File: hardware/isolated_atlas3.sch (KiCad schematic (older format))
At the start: 14 parts, among them J501 CONN_01X02, U501 adm3260, U502 ATLAS_SENSOR

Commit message: Fix SSOP-20 width on the isolator.
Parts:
- U501: footprint SMD_Packages:SSOP-20 -> conservify:SSOP20-53
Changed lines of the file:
@@
 F 0 "U501" H 4400 2750 60  0000 C CNN
 F 1 "adm3260" H 4400 2900 60  0000 C CNN
-F 2 "SMD_Packages:SSOP-20" H 4400 2900 60  0001 C CNN
+F 2 "conservify:SSOP20-53" H 4400 2900 60  0001 C CNN
 F 3 "" H 4400 2900 60  0001 C CNN
 F 4 "584-ADM3260ARSZ" H 0   0   50  0001 C CNN "spn1"

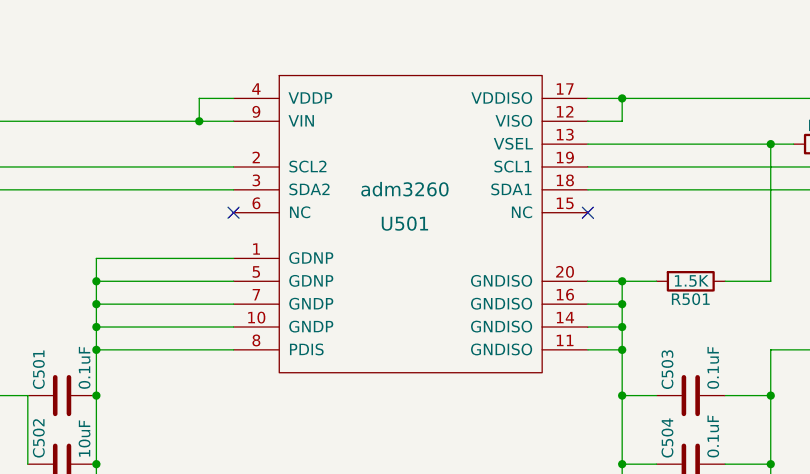
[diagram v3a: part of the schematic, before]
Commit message: Fixing some component names.
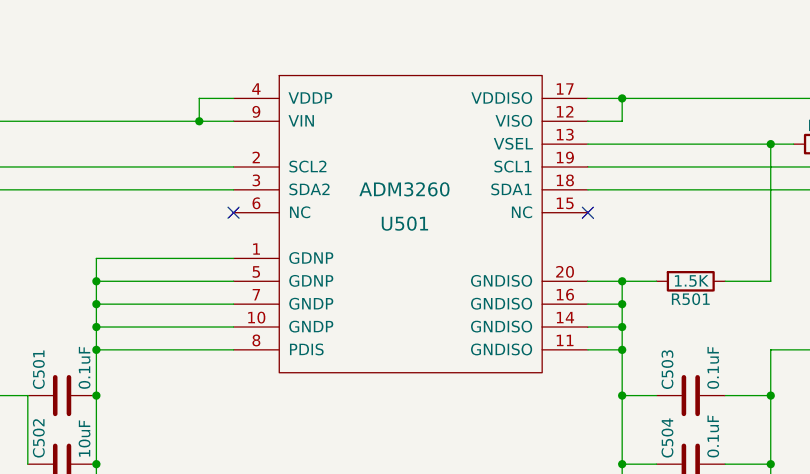
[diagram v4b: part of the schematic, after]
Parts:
- C501, C502, C503, C504, C505, C506, J501, R501, R502, R503, R504, R505, U502: price (none) -> 0
- U501: value adm3260 -> ADM3260; price (none) -> 0

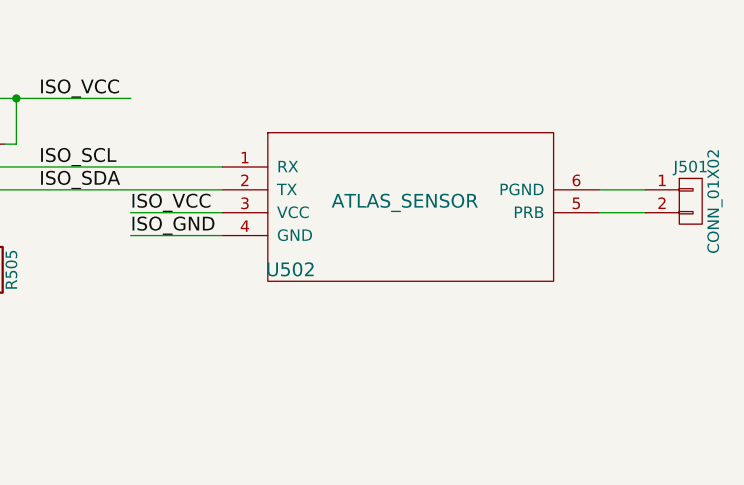
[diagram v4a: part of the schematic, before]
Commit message: Individual atlas sensor values for costing.
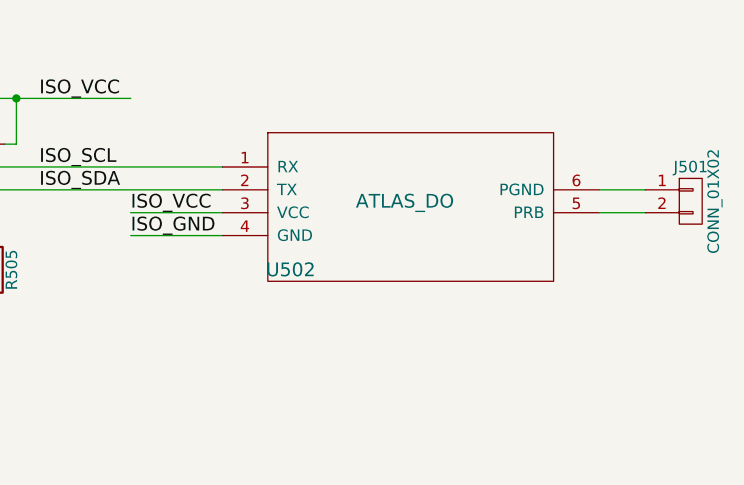
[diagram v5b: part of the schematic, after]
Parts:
- U502: value ATLAS_SENSOR -> ATLAS_DO

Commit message: Normalizing some passive footprints.
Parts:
- C501, C503, C504: footprint Resistors_SMD:R_0603_HandSoldering -> Capacitors_SMD:C_0603_HandSoldering
- C502, C505, C506: footprint Resistors_SMD:R_0603_HandSoldering -> Capacitors_SMD:C_0603_HandSoldering; spn1 810-C1608X7S0J106M -> 81-GRM188R60J106ME47

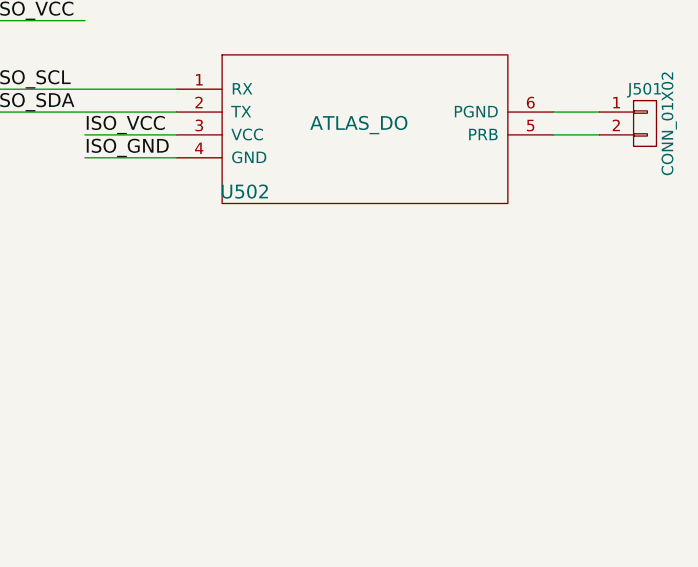
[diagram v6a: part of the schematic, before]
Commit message: Adding placeholders for probes for the BOM.
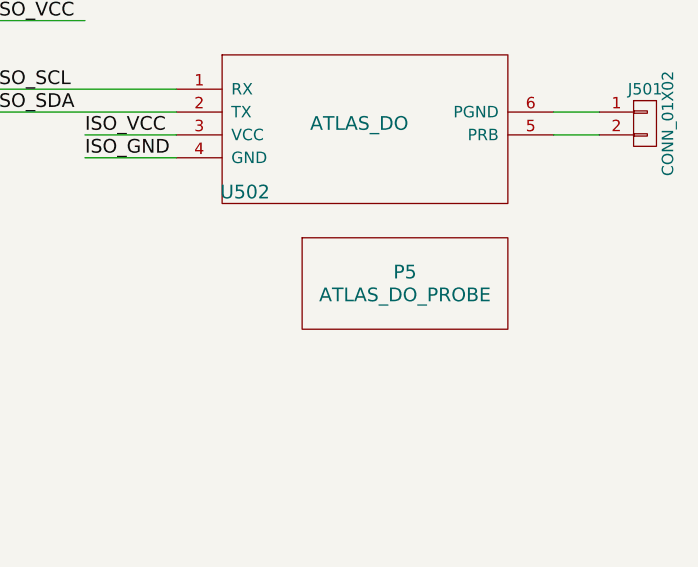
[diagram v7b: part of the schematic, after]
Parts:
- added P5: ATLAS_DO_PROBE, Oddities:Dummy_Empty, symbol WATER_PROBE

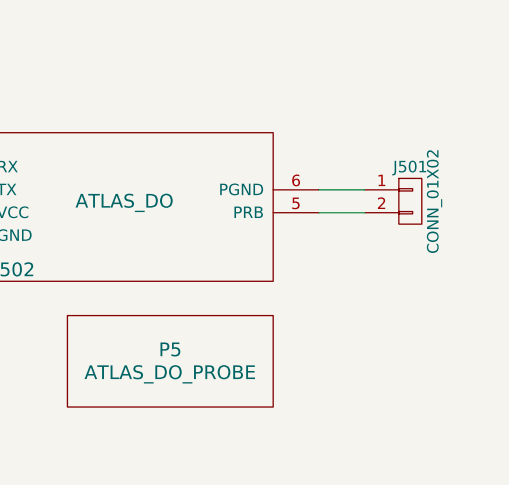
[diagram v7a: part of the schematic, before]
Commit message: Add footprint for OEM Atlas Circuit.
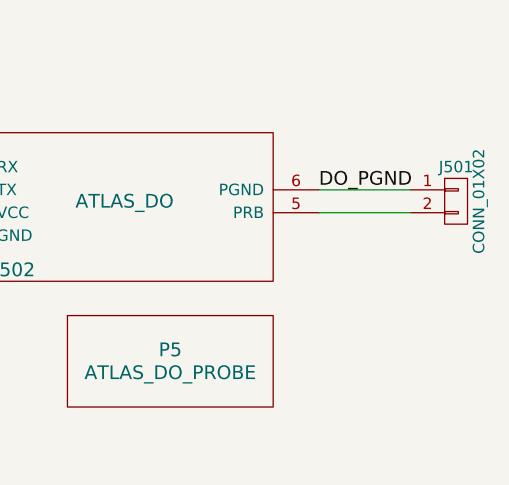
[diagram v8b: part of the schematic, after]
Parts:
- U502: footprint conservify:atlas_sensor_board -> conservify:ATLAS_SENSOR_BOARD_COMBO
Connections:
- net labels added: DO_PGND
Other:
- moved on the sheet: J501
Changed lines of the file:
@@
 F 0 "U502" H 8100 2550 60  0000 C CNN
 F 1 "ATLAS_DO" H 8600 2850 60  0000 C CNN
-F 2 "conservify:atlas_sensor_board" H 8550 2900 60  0001 C CNN
+F 2 "conservify:ATLAS_SENSOR_BOARD_COMBO" H 8550 2900 60  0001 C CNN
 F 3 "" H 8550 2900 60  0001 C CNN
 F 4 "0" H 8100 2650 50  0001 C CNN "price"
@@
 L CONN_01X02 J501
 U 1 1 594D403D
-P 9850 2950
-F 0 "J501" H 9850 3100 50  0000 C CNN
-F 1 "CONN_01X02" V 9950 2950 50  0000 C CNN
-F 2 "conservify:BNC" H 9850 2950 50  0001 C CNN
-F 3 "" H 9850 2950 50  0001 C CNN
-F 4 "0" H 9850 3200 50  0001 C CNN "price"
-F 5 "523-31-5431" H 0   0   50  0001 C CNN "spn1"
-	1    9850 2950
+P 10050 2950
+F 0 "J501" H 10050 3100 50  0000 C CNN
+F 1 "CONN_01X02" V 10150 2950 50  0000 C CNN
+F 2 "conservify:BNC" H 10050 2950 50  0001 C CNN
+F 3 "" H 10050 2950 50  0001 C CNN
+F 4 "0" H 10050 3200 50  0001 C CNN "price"
+F 5 "523-31-5431" H 200 0   50  0001 C CNN "spn1"
+	1    10050 2950
 	1    0    0    -1
 $EndComp
@@
 	7400 3000 7800 3000
 Wire Wire Line
-	9650 2900 9450 2900
+	9450 2900 9850 2900
 Wire Wire Line
-	9450 3000 9650 3000
+	9450 3000 9850 3000
 Connection ~ 5350 3500
 Connection ~ 5350 3400
@@
 	1    0    0    -1
 $EndComp
+Text Label 9450 2900 0    60   ~ 0
+DO_PGND
 $EndSCHEMATC
